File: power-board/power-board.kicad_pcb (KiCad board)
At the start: 2 copper layers, 100 x 100 mm, 44 parts, among them P1 CONN_01X04, P10 CONN_01X04, P11 CONN_01X04, P12 CONN_01X04, P13 CONN_01X04, P14 CONN_01X04, P15 CONN_01X04, P16 CONN_01X04, P17 CONN_01X04, P18 CONN_01X04, P19 CONN_01X04, P2 CONN_01X04, P20 CONN_01X04, P21 CONN_01X04, P22 CONN_01X04, P23 CONN_01X04, P24 CONN_01X04, P25 CONN_01X04, P26 CONN_01X04, P27 CONN_01X04, P28 CONN_01X04, P29 CONN_01X04, P3 CONN_01X04, P30 CONN_01X04, P31 CONN_01X04, P32 CONN_01X04, P33 CONN_01X04, P34 CONN_01X04, P35 CONN_01X04, P36 CONN_01X04, P37 CONN_01X04, P38 CONN_01X04, P39 CONN_01X04, P4 CONN_01X04, P40 CONN_01X04, P41 CONN_01X04, P5 CONN_01X04, P6 CONN_01X04, P7 CONN_01X04, P8 CONN_01X04, P9 CONN_01X04

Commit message: Move KF2510 to `oac-conn`
And reduce the dependent libraries to just that one.
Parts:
- P10, P11, P12, P13, P14, P15, P16, P17, P18, P19, P20, P21, P22, P23, P24, P25, P26, P27, P28, P29, P30, P31, P32, P33, P34, P35, P36, P37, P38, P39, P4, P5, P6, P7, P8, P9: footprint ifs-connectors:KF2510-A-4P-M-TH-V -> oac-conn:kf2510-4p

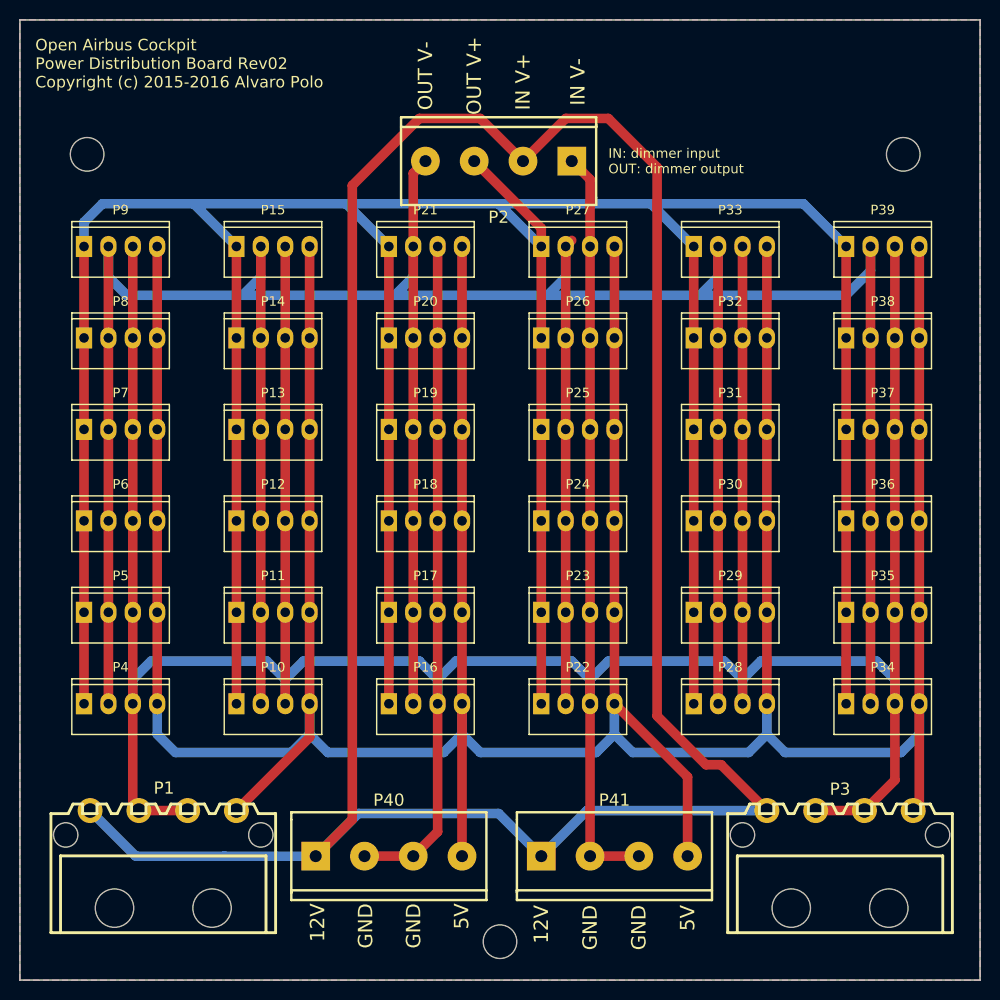
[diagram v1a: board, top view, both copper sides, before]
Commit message: Complete move 3rd party modules to `oac-conn` library
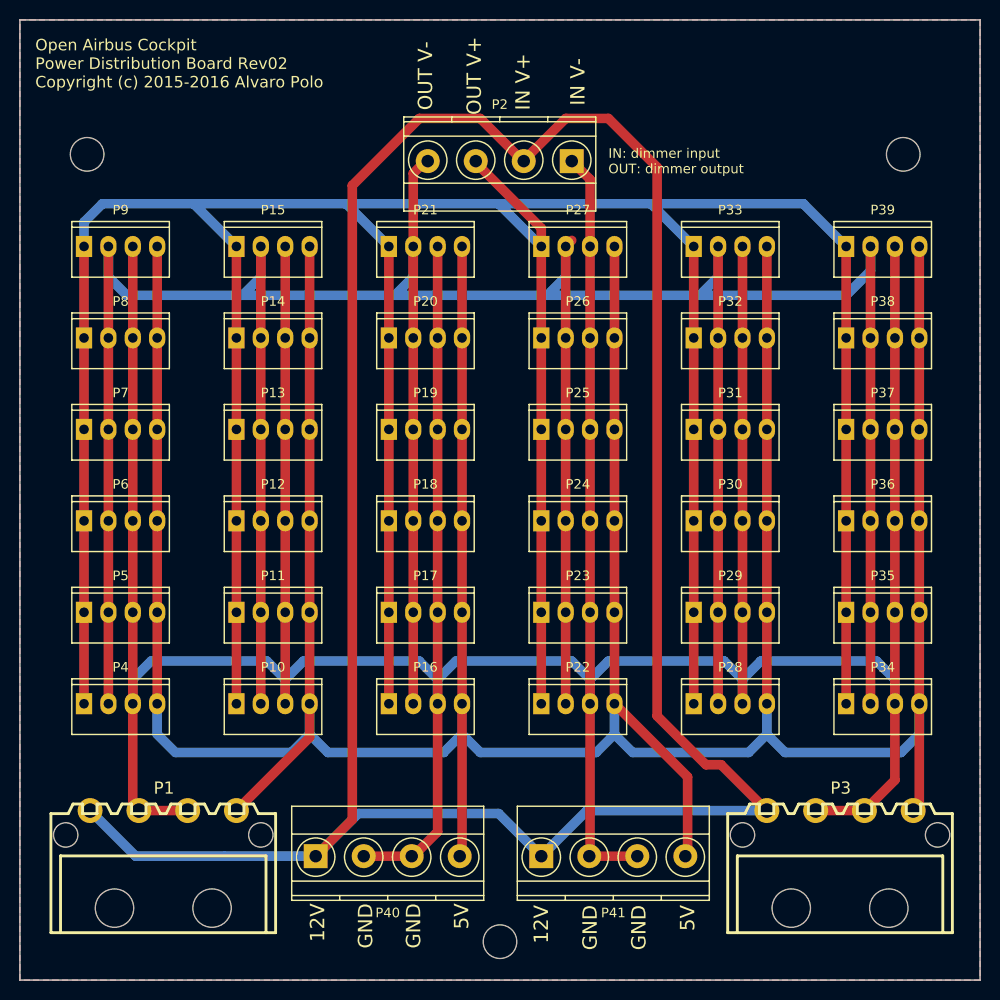
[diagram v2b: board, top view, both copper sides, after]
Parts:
- P1, P3: footprint w_conn_pc:conn_hdd_15-24-4441 -> oac-conn:molex-hdd
- P2, P40, P41: footprint w_conn_screw:mors_4p -> Terminal_Blocks:TerminalBlock_Pheonix_MKDS1.5-4pol
- moved P41 7.62 mm to (114.3, 125.1)
- moved P2 7.62 mm to (117.5, 52.7)
- moved P40 7.62 mm to (90.8, 125.1)
